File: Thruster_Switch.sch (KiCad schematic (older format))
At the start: 15 parts

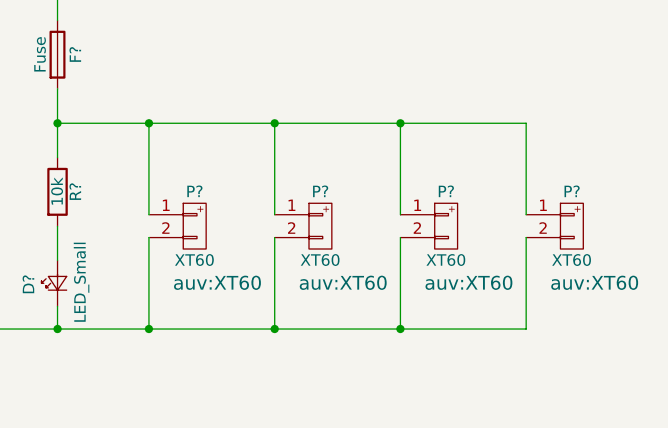
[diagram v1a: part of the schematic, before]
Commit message: Correct all foot-print assignments
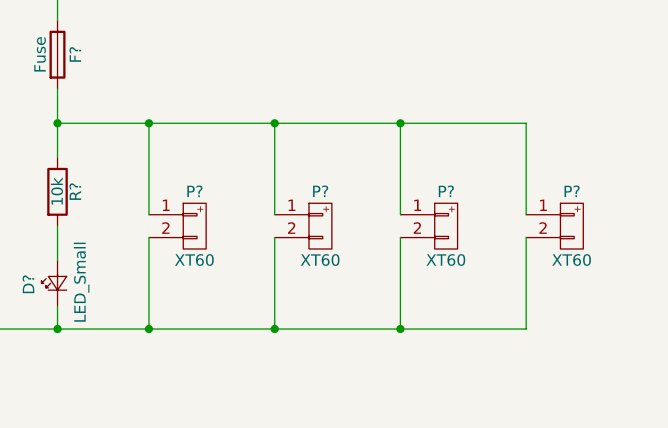
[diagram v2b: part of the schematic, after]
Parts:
- P? (x4): footprint auv:XT60 -> zeabus:XT60
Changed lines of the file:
@@
 $Descr A4 11693 8268
 encoding utf-8
-Sheet 6 12
+Sheet 11 13
 Title ""
 Date ""
@@
 AR Path="/58E52973/58E019DD" Ref="P?"  Part="1"
 AR Path="/58E62AD5/58E019DD" Ref="P?"  Part="1"
+AR Path="/58E6D43E/58E019DD" Ref="P?"  Part="1"
 F 0 "P?" H 6850 4450 50  0000 C CNN
 F 1 "XT60" H 6850 4150 50  0000 C CNN
-F 2 "auv:XT60" H 6950 4050 60  0000 C CNN
+F 2 "zeabus:XT60" H 6950 4050 60  0001 C CNN
 F 3 "" H 6850 4300 60  0000 C CNN
 	1    6850 4300
@@
 AR Path="/58E52973/58E01A68" Ref="R?"  Part="1"
 AR Path="/58E62AD5/58E01A68" Ref="R?"  Part="1"
+AR Path="/58E6D43E/58E01A68" Ref="R?"  Part="1"
 F 0 "R?" V 6330 4150 50  0000 C CNN
 F 1 "10k" V 6250 4150 50  0000 C CNN
@@
 AR Path="/58E52973/58E01A8B" Ref="D?"  Part="1"
 AR Path="/58E62AD5/58E01A8B" Ref="D?"  Part="1"
+AR Path="/58E6D43E/58E01A8B" Ref="D?"  Part="1"
 F 0 "D?" H 6200 4675 50  0000 L CNN
 F 1 "LED_Small" H 6075 4450 50  0000 L CNN
@@
 AR Path="/58E52973/58E01FA8" Ref="R?"  Part="1"
 AR Path="/58E62AD5/58E01FA8" Ref="R?"  Part="1"
+AR Path="/58E6D43E/58E01FA8" Ref="R?"  Part="1"
 F 0 "R?" V 5630 2500 50  0000 C CNN
 F 1 "10k" V 5550 2500 50  0000 C CNN
@@
 AR Path="/58E52973/58E01FFB" Ref="R?"  Part="1"
 AR Path="/58E62AD5/58E01FFB" Ref="R?"  Part="1"
+AR Path="/58E6D43E/58E01FFB" Ref="R?"  Part="1"
 F 0 "R?" V 5630 3050 50  0000 C CNN
 F 1 "100" V 5550 3050 50  0000 C CNN
@@
 AR Path="/58E52973/58E0369B" Ref="#PWR?"  Part="1"
 AR Path="/58E62AD5/58E0369B" Ref="#PWR?"  Part="1"
+AR Path="/58E6D43E/58E0369B" Ref="#PWR?"  Part="1"
 F 0 "#PWR?" H 5250 4650 50  0001 C CNN
 F 1 "GND" H 5250 4750 50  0000 C CNN
@@
 AR Path="/58E52973/58E0D2A0" Ref="P?"  Part="1"
 AR Path="/58E62AD5/58E0D2A0" Ref="P?"  Part="1"
+AR Path="/58E6D43E/58E0D2A0" Ref="P?"  Part="1"
 F 0 "P?" H 7400 4450 50  0000 C CNN
 F 1 "XT60" H 7400 4150 50  0000 C CNN
-F 2 "auv:XT60" H 7500 4050 60  0000 C CNN
+F 2 "zeabus:XT60" H 7500 4050 60  0001 C CNN
 F 3 "" H 7400 4300 60  0000 C CNN
 	1    7400 4300
@@
 AR Path="/58E52973/58E0D2E8" Ref="P?"  Part="1"
 AR Path="/58E62AD5/58E0D2E8" Ref="P?"  Part="1"
+AR Path="/58E6D43E/58E0D2E8" Ref="P?"  Part="1"
 F 0 "P?" H 7950 4450 50  0000 C CNN
 F 1 "XT60" H 7950 4150 50  0000 C CNN
-F 2 "auv:XT60" H 8050 4050 60  0000 C CNN
+F 2 "zeabus:XT60" H 8050 4050 60  0001 C CNN
 F 3 "" H 7950 4300 60  0000 C CNN
 	1    7950 4300
@@
 AR Path="/58E52973/58E0D33F" Ref="P?"  Part="1"
 AR Path="/58E62AD5/58E0D33F" Ref="P?"  Part="1"
+AR Path="/58E6D43E/58E0D33F" Ref="P?"  Part="1"
 F 0 "P?" H 8500 4450 50  0000 C CNN
 F 1 "XT60" H 8500 4150 50  0000 C CNN
-F 2 "auv:XT60" H 8600 4050 60  0000 C CNN
+F 2 "zeabus:XT60" H 8600 4050 60  0001 C CNN
 F 3 "" H 8500 4300 60  0000 C CNN
 	1    8500 4300
@@
 AR Path="/58E52973/58E4CD5F" Ref="R?"  Part="1"
 AR Path="/58E62AD5/58E4CD5F" Ref="R?"  Part="1"
+AR Path="/58E6D43E/58E4CD5F" Ref="R?"  Part="1"
 F 0 "R?" V 4080 4050 50  0000 C CNN
 F 1 "2.2k" V 4000 4050 50  0000 C CNN
@@
 AR Path="/58E52973/58E4F6EC" Ref="Q?"  Part="1"
 AR Path="/58E62AD5/58E4F6EC" Ref="Q?"  Part="1"
+AR Path="/58E6D43E/58E4F6EC" Ref="Q?"  Part="1"
 F 0 "Q?" H 5350 4125 50  0000 L CNN
 F 1 "BC817-40" H 5350 4050 50  0000 L CNN
@@
 AR Path="/58E52973/58E4FE30" Ref="F?"  Part="1"
 AR Path="/58E62AD5/58E4FE30" Ref="F?"  Part="1"
+AR Path="/58E6D43E/58E4FE30" Ref="F?"  Part="1"
 F 0 "F?" V 6330 3550 50  0000 C CNN
 F 1 "Fuse" V 6175 3550 50  0000 C CNN
@@
 AR Path="/58E52973/58E515C3" Ref="D?"  Part="1"
 AR Path="/58E62AD5/58E515C3" Ref="D?"  Part="1"
+AR Path="/58E6D43E/58E515C3" Ref="D?"  Part="1"
 F 0 "D?" H 4250 4450 50  0000 C CNN
 F 1 "MBR0530T3G" H 4250 4250 50  0000 C CNN
@@
 AR Path="/58E52973/58E53CD9" Ref="C?"  Part="1"
 AR Path="/58E62AD5/58E53CD9" Ref="C?"  Part="1"
+AR Path="/58E6D43E/58E53CD9" Ref="C?"  Part="1"
 F 0 "C?" H 4625 4450 50  0000 L CNN
 F 1 "1uF" H 4625 4250 50  0000 L CNN
@@
 AR Path="/58E52973/58E51C6A" Ref="Q?"  Part="1"
 AR Path="/58E62AD5/58E51C6A" Ref="Q?"  Part="1"
+AR Path="/58E6D43E/58E51C6A" Ref="Q?"  Part="1"
 F 0 "Q?" H 6350 3100 50  0000 L CNN
 F 1 "IPI120P04P4L" H 6350 3000 50  0000 L CNN
@@
 AR Path="/58E52973/58E67103" Ref="R?"  Part="1"
 AR Path="/58E62AD5/58E67103" Ref="R?"  Part="1"
+AR Path="/58E6D43E/58E67103" Ref="R?"  Part="1"
 F 0 "R?" V 5330 4500 50  0000 C CNN
 F 1 "10K" V 5250 4500 50  0000 C CNN

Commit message: Annotate all components
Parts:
- gave numbers to parts that had none: 15

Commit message: Bug fixed and clean-up for PCB generating
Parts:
- removed R9: 10K, Resistors_SMD:R_0603, symbol R
- added D2: BZX585-C12, Diodes_SMD:D_SOD-523, symbol D_Zener
- added R2: 330, Resistors_SMD:R_0603, symbol R
- F1: footprint auv:FUSE_AUTO -> zeabus:FUSE_AUTO
- Q2: renamed from Q4; value IPI120P04P4L -> IPD90P03P4L; footprint TO_SOT_Packages_SMD:TO-263-3Lead -> TO_SOT_Packages_SMD:TO-252-2Lead
- R4: renamed from R11; value 100 -> 1k
- renumbered D6 to D1, D7 to D3, P8 to P1, P9 to P2, P10 to P3, P11 to P4, Q3 to Q1, R8 to R1, R10 to R3, R12 to R5
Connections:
- wire segments 30 -> 32
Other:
- moved on the sheet: C6

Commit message: Bug fixed in DC-DC Converter and removed unused files.
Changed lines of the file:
@@
 AR Path="/58E6D43E/58E019DD" Ref="P11"  Part="1"
 AR Path="/58E0048C/58E019DD" Ref="P15"  Part="1"
-F 0 "P15" H 6850 4450 50  0000 C CNN
+F 0 "P1" H 6850 4450 50  0000 C CNN
 F 1 "XT60" H 6850 4150 50  0000 C CNN
 F 2 "zeabus:XT60" H 6950 4050 60  0001 C CNN
@@
 AR Path="/58E6D43E/58E01A68" Ref="R25"  Part="1"
 AR Path="/58E0048C/58E01A68" Ref="R30"  Part="1"
-F 0 "R30" V 6330 4150 50  0000 C CNN
+F 0 "R5" V 6330 4150 50  0000 C CNN
 F 1 "10k" V 6250 4150 50  0000 C CNN
 F 2 "Resistors_SMD:R_0603" V 6180 4150 50  0001 C CNN
@@
 AR Path="/58E6D43E/58E01A8B" Ref="D13"  Part="1"
 AR Path="/58E0048C/58E01A8B" Ref="D16"  Part="1"
-F 0 "D16" H 6200 4675 50  0000 L CNN
+F 0 "D3" H 6200 4675 50  0000 L CNN
 F 1 "LED_Small" H 6075 4450 50  0000 L CNN
 F 2 "LEDs:LED_0603" V 6250 4550 50  0001 C CNN
@@
 AR Path="/58E6D43E/58E01FA8" Ref="R23"  Part="1"
 AR Path="/58E0048C/58E01FA8" Ref="R28"  Part="1"
-F 0 "R28" V 5630 2500 50  0000 C CNN
+F 0 "R3" V 5630 2500 50  0000 C CNN
 F 1 "10k" V 5550 2500 50  0000 C CNN
 F 2 "Resistors_SMD:R_0603" V 5480 2500 50  0001 C CNN
@@
 AR Path="/58E6D43E/58E01FFB" Ref="R24"  Part="1"
 AR Path="/58E0048C/58E01FFB" Ref="R29"  Part="1"
-F 0 "R29" V 5630 3050 50  0000 C CNN
+F 0 "R4" V 5630 3050 50  0000 C CNN
 F 1 "1k" V 5550 3050 50  0000 C CNN
 F 2 "Resistors_SMD:R_0603" V 5480 3050 50  0001 C CNN
@@
 AR Path="/58E6D43E/58E0369B" Ref="#PWR20"  Part="1"
 AR Path="/58E0048C/58E0369B" Ref="#PWR21"  Part="1"
-F 0 "#PWR21" H 5250 4650 50  0001 C CNN
+F 0 "#PWR16" H 5250 4650 50  0001 C CNN
 F 1 "GND" H 5250 4750 50  0000 C CNN
 F 2 "" H 5250 4900 50  0001 C CNN
@@
 AR Path="/58E6D43E/58E0D2A0" Ref="P12"  Part="1"
 AR Path="/58E0048C/58E0D2A0" Ref="P16"  Part="1"
-F 0 "P16" H 7400 4450 50  0000 C CNN
+F 0 "P2" H 7400 4450 50  0000 C CNN
 F 1 "XT60" H 7400 4150 50  0000 C CNN
 F 2 "zeabus:XT60" H 7500 4050 60  0001 C CNN
@@
 AR Path="/58E6D43E/58E0D2E8" Ref="P13"  Part="1"
 AR Path="/58E0048C/58E0D2E8" Ref="P17"  Part="1"
-F 0 "P17" H 7950 4450 50  0000 C CNN
+F 0 "P3" H 7950 4450 50  0000 C CNN
 F 1 "XT60" H 7950 4150 50  0000 C CNN
 F 2 "zeabus:XT60" H 8050 4050 60  0001 C CNN
@@
 AR Path="/58E6D43E/58E0D33F" Ref="P14"  Part="1"
 AR Path="/58E0048C/58E0D33F" Ref="P18"  Part="1"
-F 0 "P18" H 8500 4450 50  0000 C CNN
+F 0 "P4" H 8500 4450 50  0000 C CNN
 F 1 "XT60" H 8500 4150 50  0000 C CNN
 F 2 "zeabus:XT60" H 8600 4050 60  0001 C CNN
@@
 AR Path="/58E6D43E/58E4CD5F" Ref="R21"  Part="1"
 AR Path="/58E0048C/58E4CD5F" Ref="R26"  Part="1"
-F 0 "R26" V 4080 4050 50  0000 C CNN
+F 0 "R1" V 4080 4050 50  0000 C CNN
 F 1 "2.2k" V 4000 4050 50  0000 C CNN
 F 2 "Resistors_SMD:R_0603" V 3930 4050 50  0001 C CNN
@@
 AR Path="/58E6D43E/58E4F6EC" Ref="Q9"  Part="1"
 AR Path="/58E0048C/58E4F6EC" Ref="Q11"  Part="1"
-F 0 "Q11" H 5350 4125 50  0000 L CNN
+F 0 "Q1" H 5350 4125 50  0000 L CNN
 F 1 "BC817-40" H 5350 4050 50  0000 L CNN
 F 2 "TO_SOT_Packages_SMD:SOT-23" H 5350 3975 50  0001 L CIN
@@
 AR Path="/58E6D43E/58E4FE30" Ref="F5"  Part="1"
 AR Path="/58E0048C/58E4FE30" Ref="F6"  Part="1"
-F 0 "F6" V 6330 3550 50  0000 C CNN
+F 0 "F1" V 6330 3550 50  0000 C CNN
 F 1 "Fuse" V 6175 3550 50  0000 C CNN
 F 2 "zeabus:FUSE_AUTO" V 6180 3550 50  0001 C CNN
@@
 AR Path="/58E6D43E/58E515C3" Ref="D11"  Part="1"
 AR Path="/58E0048C/58E515C3" Ref="D14"  Part="1"
-F 0 "D14" H 4250 4450 50  0000 C CNN
+F 0 "D1" H 4250 4450 50  0000 C CNN
 F 1 "MBR0530T3G" H 4250 4250 50  0000 C CNN
 F 2 "Diodes_SMD:D_SOD-123" H 4250 4350 50  0001 C CNN
@@
 AR Path="/58E6D43E/58E53CD9" Ref="C5"  Part="1"
 AR Path="/58E0048C/58E53CD9" Ref="C6"  Part="1"
-F 0 "C6" H 4525 4450 50  0000 L CNN
+F 0 "C1" H 4525 4450 50  0000 L CNN
 F 1 "1uF" H 4525 4250 50  0000 L CNN
 F 2 "Capacitors_SMD:C_0603" H 4538 4200 50  0001 C CNN
@@
 AR Path="/58E6D43E/58E51C6A" Ref="Q10"  Part="1"
 AR Path="/58E0048C/58E51C6A" Ref="Q12"  Part="1"
-F 0 "Q12" H 6350 3100 50  0000 L CNN
+F 0 "Q2" H 6350 3100 50  0000 L CNN
 F 1 "IPD90P03P4L" H 6350 3000 50  0000 L CNN
 F 2 "TO_SOT_Packages_SMD:TO-252-2Lead" H 6350 3150 50  0001 C CNN
@@
 AR Path="/58E6D43E/58E6316B" Ref="R22"  Part="1"
 AR Path="/58E0048C/58E6316B" Ref="R27"  Part="1"
-F 0 "R27" V 4780 4050 50  0000 C CNN
+F 0 "R2" V 4780 4050 50  0000 C CNN
 F 1 "330" V 4700 4050 50  0000 C CNN
 F 2 "Resistors_SMD:R_0603" V 4630 4050 50  0001 C CNN
@@
 AR Path="/58E6D43E/58E6427A" Ref="D12"  Part="1"
 AR Path="/58E0048C/58E6427A" Ref="D15"  Part="1"
-F 0 "D15" H 5850 2850 50  0000 C CNN
+F 0 "D2" H 5850 2850 50  0000 C CNN
 F 1 "BZX585-C12" H 5850 2650 50  0000 C CNN
 F 2 "Diodes_SMD:D_SOD-523" H 5850 2750 50  0001 C CNN
